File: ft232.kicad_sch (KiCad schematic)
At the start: 51 parts, among them J1 FT232RL, J12 tp, J13 tp, J15 tp, J16 tp, J17 tp, J19 tp, J2 tp_ft232_, J20 tp, J24 tp, J3 USB_B_Mini, J4 tp_ft232_, J8 tp, Q14 FDN306P, U13 FT232RL, U4 LM1117DT-3.3, Y3 Crystal_GND24_Small_12MHZ

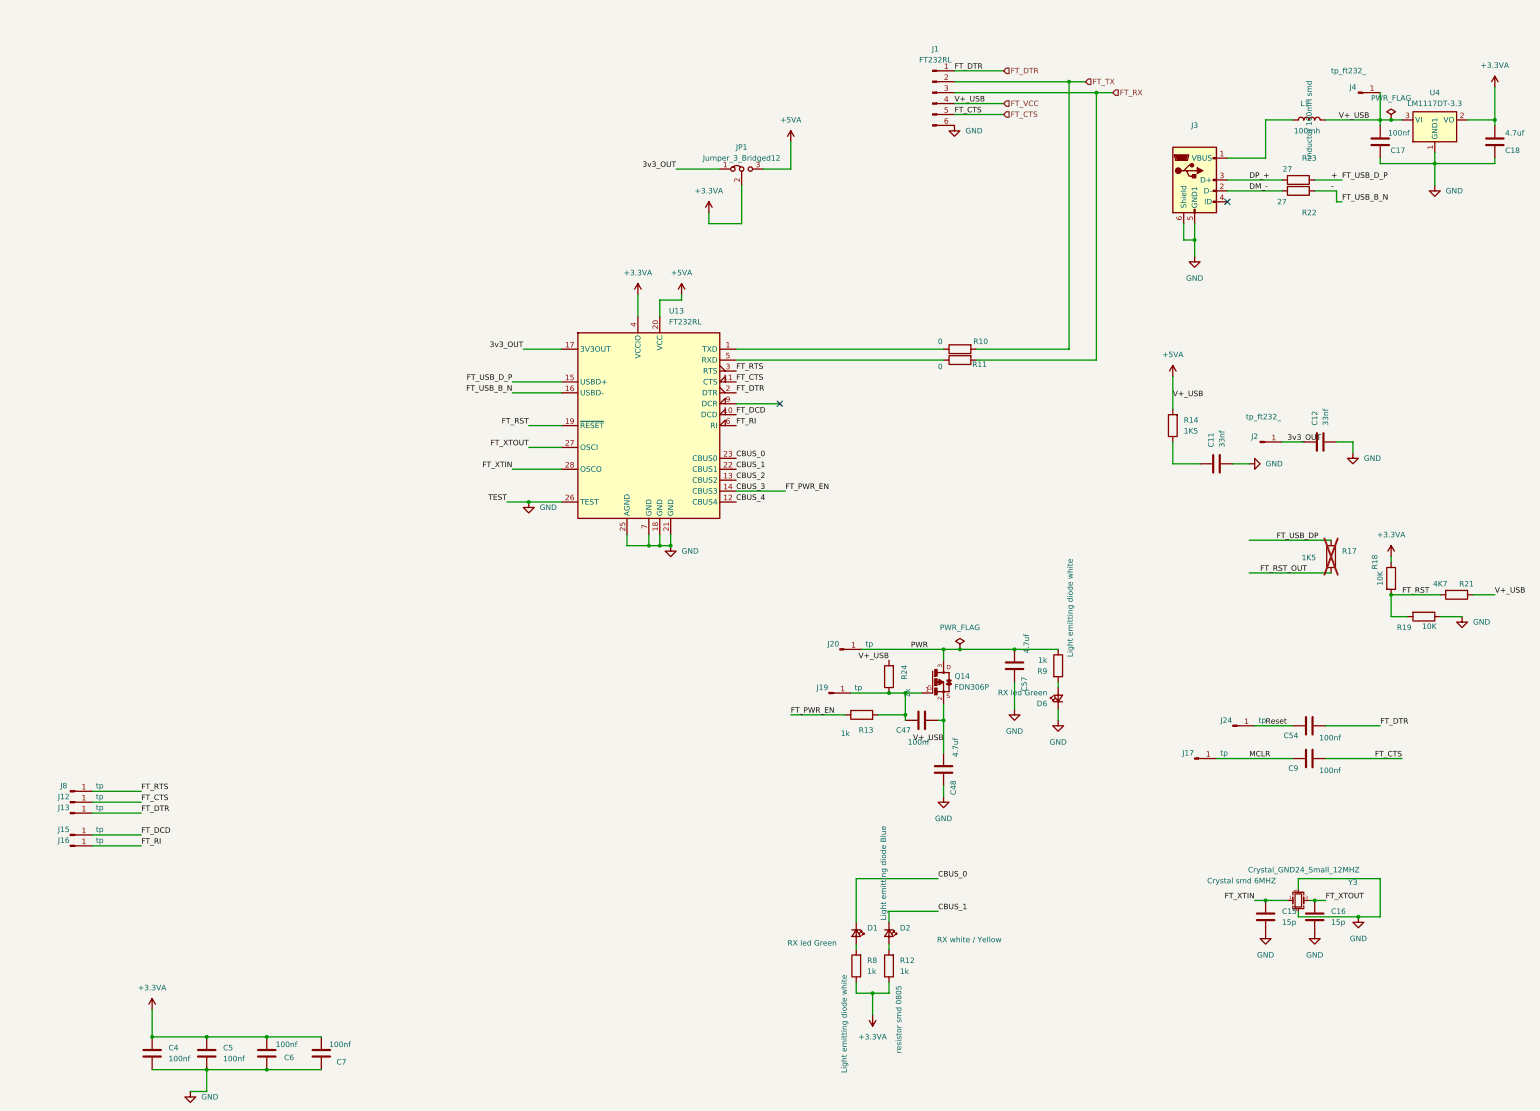
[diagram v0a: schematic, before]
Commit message: adptador de ft232bm
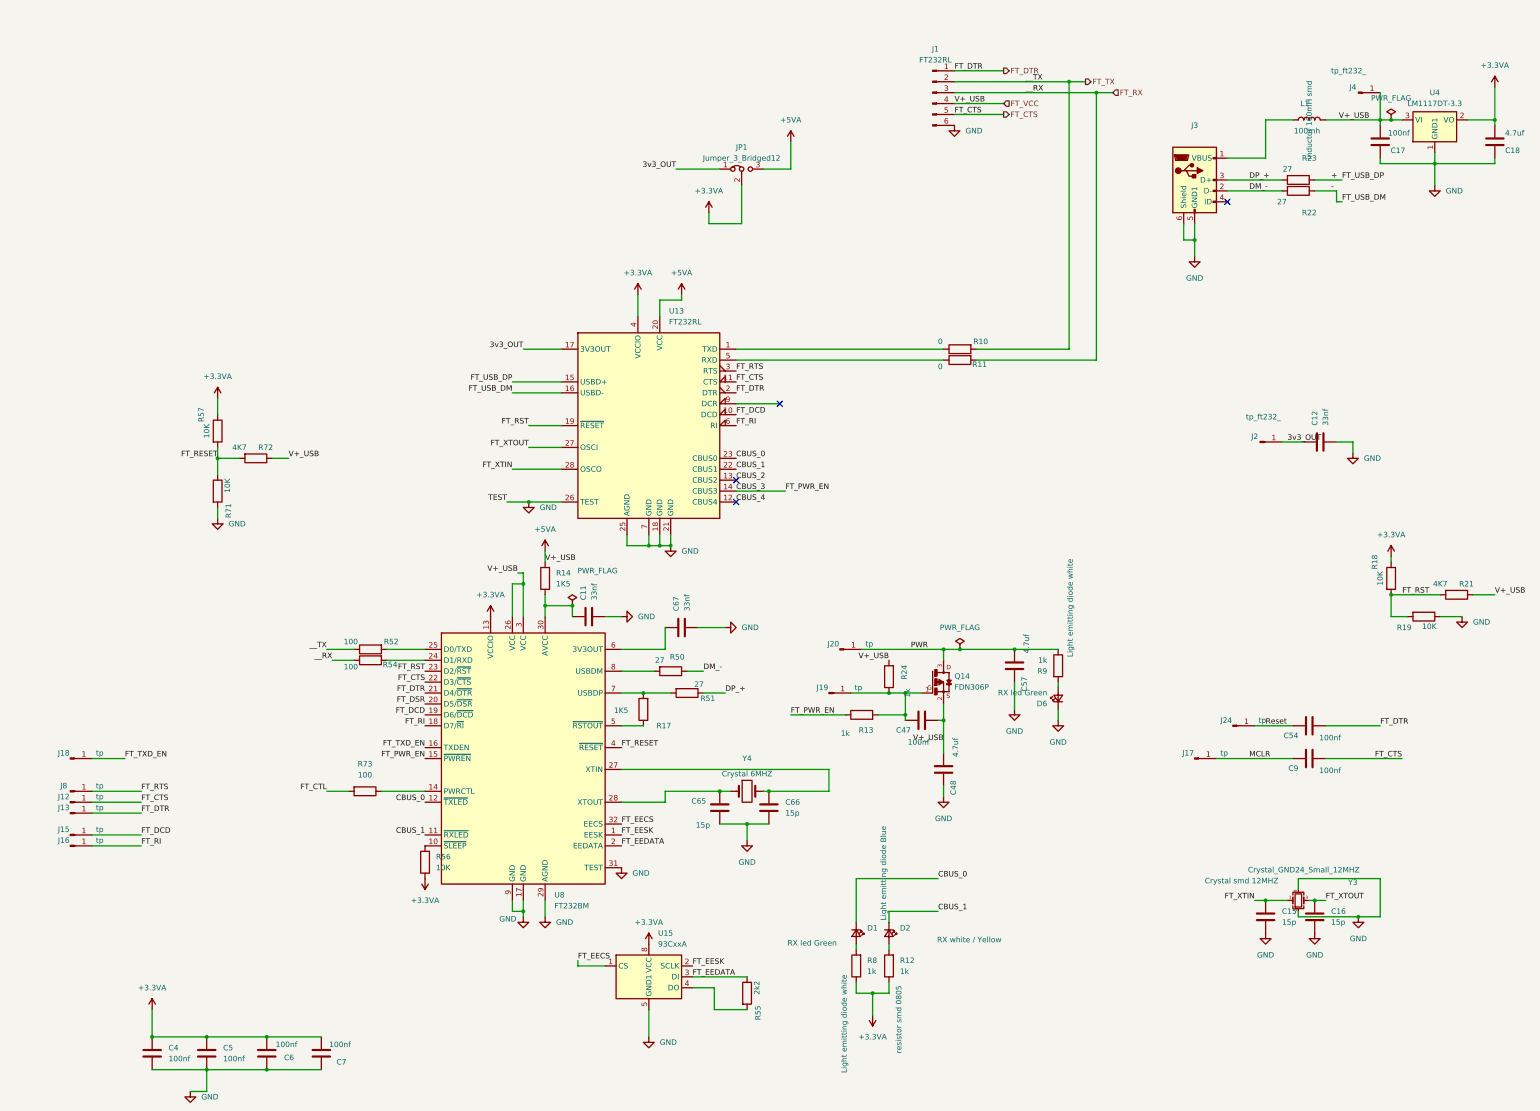
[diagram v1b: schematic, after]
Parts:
- added C65, C66: 15p, Capacitor_SMD:C_0805_2012Metric, symbol Device:C
- added C67: 33nf, Capacitor_SMD:C_0805_2012Metric, symbol Device:C
- added J18: tp, TestPoint:TestPoint_THTPad_1.0x1.0mm_Drill0.5mm, symbol Connector:Conn_01x01_Pin
- added R50, R51: 27, Resistor_SMD:R_0805_2012Metric, symbol Device:R
- added R52, R54, R73: 100, Resistor_SMD:R_0805_2012Metric, symbol Device:R
- added R55: 2k2, Resistor_SMD:R_0805_2012Metric, symbol Device:R
- added R56, R57, R71: 10K, Resistor_SMD:R_0805_2012Metric, symbol Device:R
- added R72: 4K7, Resistor_SMD:R_0805_2012Metric, symbol Device:R
- added U15: 93CxxA, Package_SO:SOIC-8_7.5x5.85mm_P1.27mm, symbol Memory_EEPROM:93CxxA
- added U8: FT232BM, Package_QFP:LQFP-32_7x7mm_P0.8mm, symbol Interface_USB:FT232BM
- added Y4: Crystal 6MHZ, Crystal:Crystal_SMD_HC49-SD, symbol Device:Crystal
- R14: now left out of the parts list
- R17: now fitted
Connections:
- net +3.3VA: now also R56.1, R57.1, U15.8 (VCC), U8.13 (VCCIO)
- net +5VA: now also R72.1, U8.26 (VCC), U8.3 (VCC)
- net CBUS_0: now also U8.12 (~{TXLED})
- net CBUS_1: now also U8.11 (~{RXLED})
- net CBUS_3: now also U8.15 (~{PWREN})
- net DM_-: now also R50.1
- net DP_+: now also R51.1
- net FT_CTS: now also U8.22 (D3/~{CTS})
- net FT_DCD: now also U8.19 (D6/~{DCD})
- net FT_DTR: now also U8.21 (D4/~{DTR})
- net FT_RI: now also U8.18 (D7/~{RI})
- net FT_RST: now also U8.23 (D2/~{RST})
- net FT_RX: now also R54.1
- net FT_TX: now also R52.1
- net GND: now also C65.2, C66.2, C67.2, R71.2, U15.5 (GND1), U8.17 (GND), U8.29 (AGND), U8.31 (TEST), U8.9 (GND)
- net at C11.1, R14.1: now also U8.30 (AVCC)
- net FT_RST_OUT: no longer names the net of R17.1
- net FT_RST_OUT: now also U8.5 (~{RSTOUT})
- net FT_USB_DP: no longer names the net of R17.2
- net FT_USB_DP: now also R51.2, U8.7 (USBDP)
- new net: C65.1, U8.28 (XTOUT), Y4.1
- new net: R56.2, U8.10 (~{SLEEP})
- new net: C67.1, U8.6 (3V3OUT)
- new net: R55.2, U15.4 (DO)
- new net: R73.1, U8.14 (PWRCTL)
- new net: R54.2, U8.24 (D1/RXD)
- new net: R52.2, U8.25 (D0/TXD)
- new net: C66.1, U8.27 (XTIN), Y4.2
- new net: R50.2, U8.8 (USBDM)
- new net FT_CTL: R73.2
- new net FT_DSR: U8.20 (D5/~{DSR})
- new net FT_EECS: U15.1 (CS), U8.32 (EECS)
- new net FT_EEDATA: R55.1, U15.3 (DI), U8.2 (EEDATA)
- new net FT_EESK: U15.2 (SCLK), U8.1 (EESK)
- new net FT_RESET: R57.2, R71.1, R72.2, U8.4 (~{RESET})
- new net FT_TXD_EN: J18.1 (Pin_1), U8.16 (TXDEN)
- no-connect marks 2 -> 4
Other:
- moved on the sheet: C11, R14

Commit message: update epaper and mt48
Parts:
- added C68, C69: 100nf, Capacitor_SMD:C_0805_2012Metric, symbol Device:C
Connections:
- net +3.3VA: now also C68.1, C69.1
- net GND: now also C68.2, C69.2

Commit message: actualizacion  de pcb logic , rpi
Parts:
- Q14: Package TO-236-3 ON -> (none)
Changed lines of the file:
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@@
-			)
-		)
-		(property "Package" "TO-236-3 ON"
-			(at 250.19 167.64 0)
-			(hide yes)
-			(show_name no)
-			(do_not_autoplace no)
-			(effects
-				(font
-					(size 1.27 1.27)
-				)
-				(justify bottom)
 			)
 		)

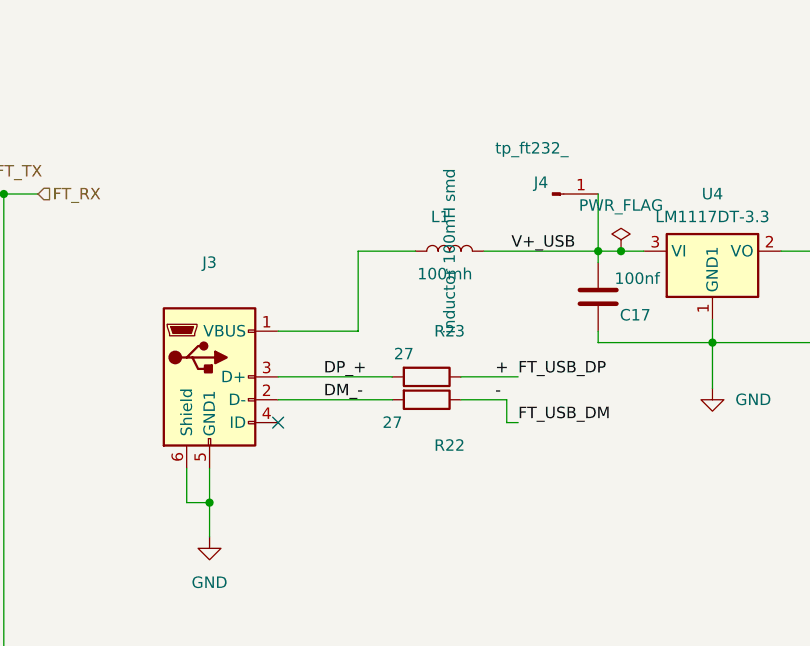
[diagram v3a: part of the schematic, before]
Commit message: correccion de numero de partes de componentes
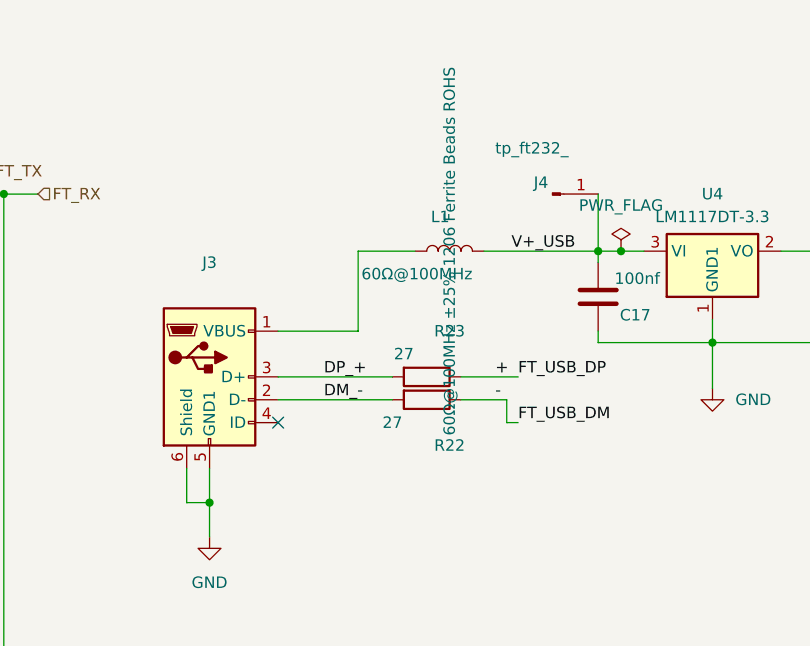
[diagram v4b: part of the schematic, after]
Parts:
- L1: value 100mh -> 60Ω@100MHz
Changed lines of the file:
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@@
 		(in_bom no)
 		(on_board yes)
-		(in_pos_files yes)
+		(in_pos_files no)
 		(dnp no)
 		(property "Reference" "J24"
@@
 		(in_bom no)
 		(on_board yes)
-		(in_pos_files yes)
+		(in_pos_files no)
 		(dnp no)
 		(property "Reference" "J2"
@@
 		(in_bom no)
 		(on_board yes)
-		(in_pos_files yes)
+		(in_pos_files no)
 		(dnp no)
 		(fields_autoplaced yes)
@@
 			)
 		)
-		(property "Value" "100mh"
+		(property "Value" "60Ω@100MHz"
 			(at 337.82 39.37 90)
 			(show_name no)
@@
 			)
 		)
-		(property "Description" "inductor 100mH smd"
+		(property "Description" "60Ω@100MHz ±25% 1206 Ferrite Beads ROHS"
 			(at 335.28 36.83 0)
 			(show_name no)
@@
 		(in_bom no)
 		(on_board yes)
-		(in_pos_files yes)
+		(in_pos_files no)
 		(dnp no)
 		(fields_autoplaced yes)
@@
 		(in_bom no)
 		(on_board yes)
-		(in_pos_files yes)
+		(in_pos_files no)
 		(dnp no)
 		(property "Reference" "J4"

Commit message: update sch & pcb
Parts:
- J3: value USB_B_Mini -> U-M-M5SS-W-2
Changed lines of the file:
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@@
 			)
 		)
-		(property "Value" "USB_B_Mini"
+		(property "Value" "U-M-M5SS-W-2"
 			(at 308.61 40.64 0)
 			(hide yes)
